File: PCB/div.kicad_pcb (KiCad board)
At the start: 2 copper layers, 31.5 x 110.5 mm, 74 parts, among them J1 Rst, J10 OUT, J2 Bus Gate Reset, J3 Clk, J4 PWR, J5 OUT, J6 OUT, J7 OUT, J8 OUT, J9 OUT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

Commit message: :memo: Change PCB text to v1.1
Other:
- board text added: "Control Board v1.1"
- board text removed: "Control Board v1"
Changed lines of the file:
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@@
   (gr_line (start 146.2 80.756) (end 146.5 80.756)
     (stroke (width 0.1) (type default)) (layer "Edge.Cuts"))
-  (gr_text "https://github.com/moPsy-project/div" (at 141.224 89.281 90) (layer "B.SilkS")
-    (effects (font (size 1 1) (thickness 0.15)) (justify left bottom mirror))
+  (gr_text "https://github.com/moPsy-project/div" (at 141.351 119.38 90) (layer "B.SilkS")
+    (effects (font (size 1 1) (thickness 0.15)) (justify right bottom mirror))
   )
   (gr_text "Jumper:\nBus Gate\nto Reset" (at 141.351 48.8 90) (layer "B.SilkS")
     (effects (font (size 1 1) (thickness 0.15)) (justify left bottom mirror))
   )
-  (gr_text "Control Board v1" (at 142.875 106.426 90) (layer "B.SilkS")
-    (effects (font (size 1 1) (thickness 0.15)) (justify left bottom mirror))
+  (gr_text "Control Board v1.1" (at 143.002 119.38 90) (layer "B.SilkS")
+    (effects (font (size 1 1) (thickness 0.15)) (justify right bottom mirror))
   )
-  (gr_text "Bend LEDs\nhere" (at 139.466 80.528) (layer "B.SilkS")
+  (gr_text "Bend LEDs\nhere" (at 139.573 80.137) (layer "B.SilkS")
     (effects (font (size 0.6 0.6) (thickness 0.1) bold) (justify bottom mirror))
   )
@@
   (segment (start 117.7032 79.0461) (end 124.7889 79.0461) (width 0.2032) (layer "F.Cu") (net 9))
   (segment (start 116.8 78.1429) (end 117.7032 79.0461) (width 0.2032) (layer "F.Cu") (net 9))
-  (segment (start 135.763 78.105) (end 134.2182 76.5602) (width 0.2032) (layer "B.Cu") (net 9))
-  (segment (start 128.0755 76.5602) (end 126.9282 75.4129) (width 0.2032) (layer "B.Cu") (net 9))
-  (segment (start 134.2182 76.5602) (end 128.0755 76.5602) (width 0.2032) (layer "B.Cu") (net 9))
+  (segment (start 128.2233 76.708) (end 126.9282 75.4129) (width 0.2032) (layer "B.Cu") (net 9))
+  (segment (start 135.763 78.105) (end 134.366 76.708) (width 0.2032) (layer "B.Cu") (net 9))
   (segment (start 135.763 79.248) (end 135.763 78.105) (width 0.2032) (layer "B.Cu") (net 9))
+  (segment (start 134.366 76.708) (end 128.2233 76.708) (width 0.2032) (layer "B.Cu") (net 9))
   (segment (start 130.683 74.041) (end 130.683 73.787) (width 0.2032) (layer "F.Cu") (net 10))
   (segment (start 125.825 73.9761) (end 126.9282 72.8729) (width 0.2032) (layer "F.Cu") (net 10))

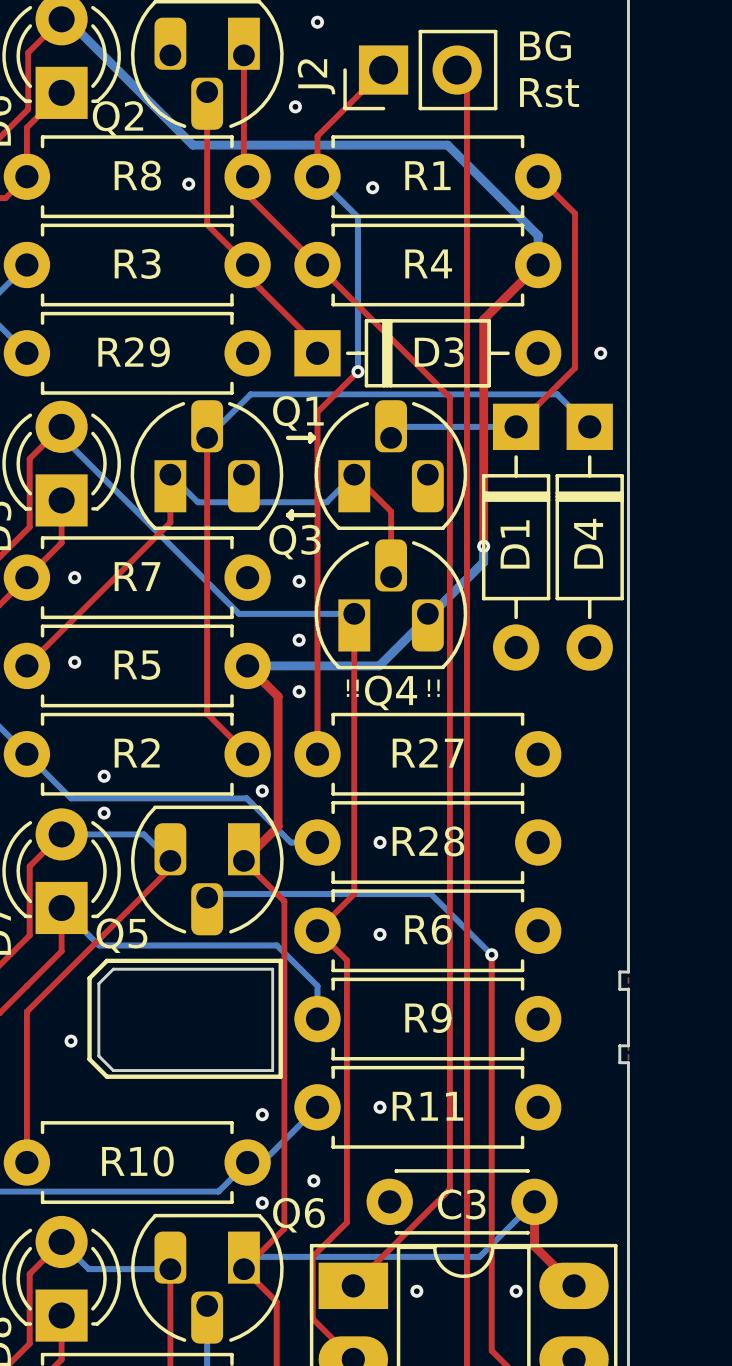
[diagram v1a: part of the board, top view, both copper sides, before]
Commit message: :art: Change the diode footprint to make soldering easier
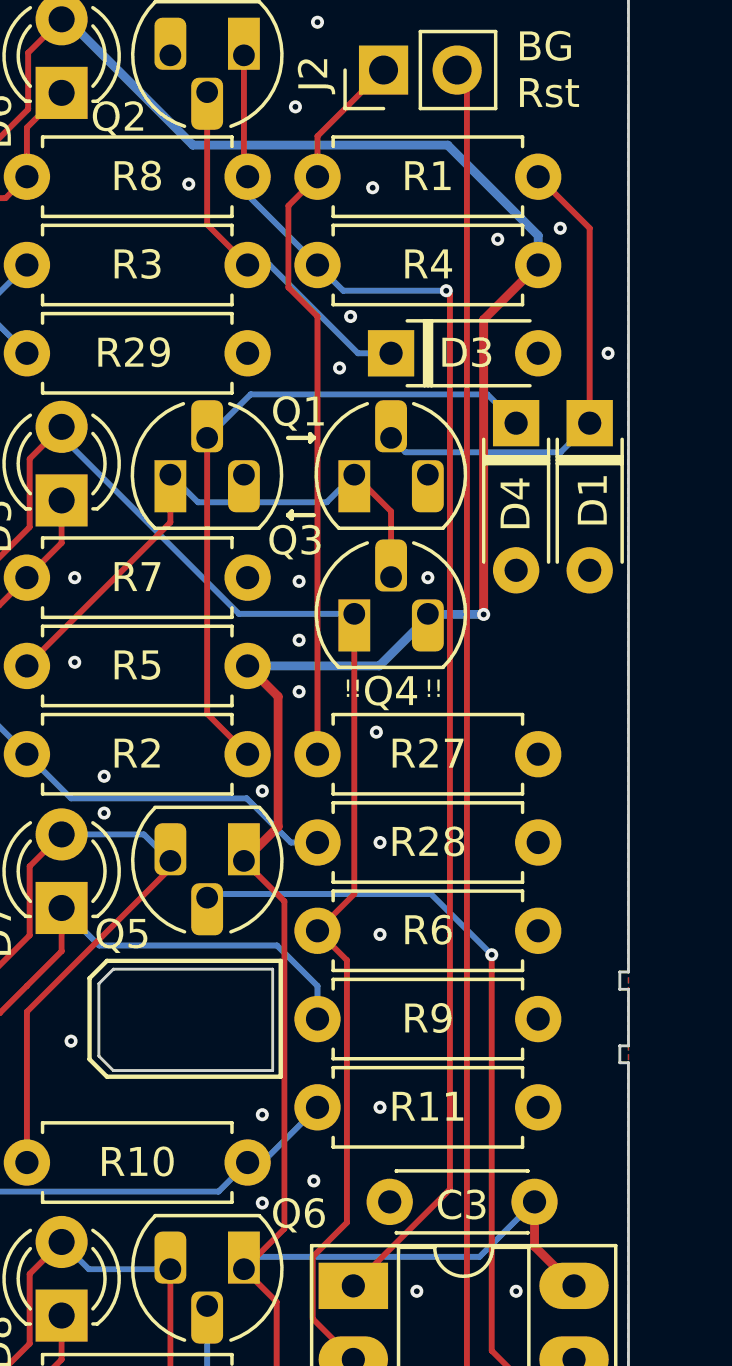
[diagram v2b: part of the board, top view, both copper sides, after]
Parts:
- D1, D3, D4: footprint Diode_THT:D_DO-35_SOD27_P7.62mm_Horizontal -> moPsy:D_DO-35_SOD27_P5.08mm_Horizontal
- moved D1 2.54 mm to (145.2, 58.7)
- moved D4 2.54 mm to (142.6, 58.7)
- moved D3 2.54 mm to (138.3, 56.3)
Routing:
- net Net-(D1-K): track 14.5 -> 17.3 mm
- net Net-(D4-K): track 25.8 -> 23.2 mm
- net Net-(D3-K): track 10.6 -> 12.7 mm
- net /CLOCK_IN: track 46.8 -> 48.9 mm, vias 0 -> 1
- net +12V: track 154.5 -> 155.6 mm
- net Net-(J2-Pin_1): track 25.7 -> 25.4 mm, vias 1 -> 0
- net GND: vias 58 -> 64

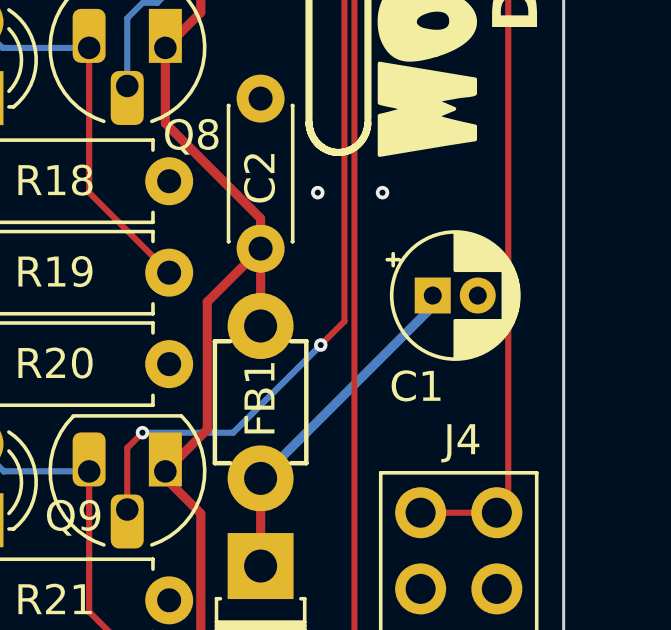
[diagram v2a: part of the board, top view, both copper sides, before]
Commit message: :art: Move C1 slightly for a more relaxed fit with the power connector
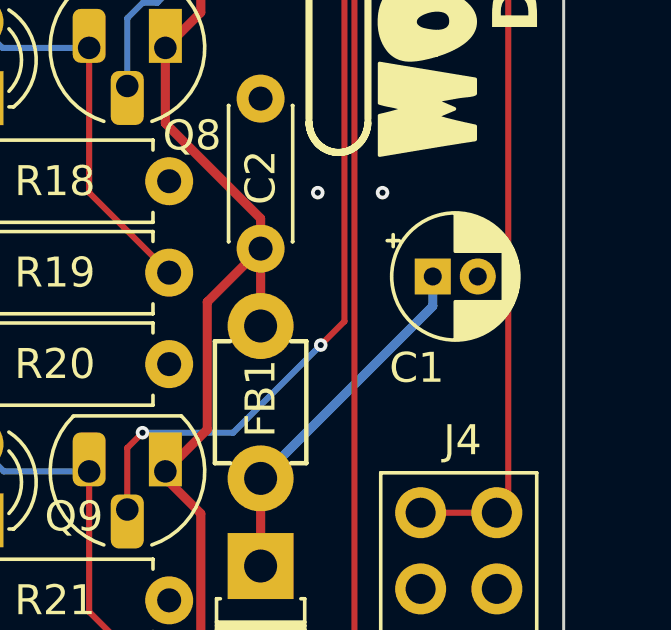
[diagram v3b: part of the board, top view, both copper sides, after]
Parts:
- moved C1 0.64 mm to (142.1, 123.6)
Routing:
- net Net-(D2-K): track 11.4 -> 12.0 mm
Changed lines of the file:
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@@
   )
   (footprint "Capacitor_THT:CP_Radial_D4.0mm_P1.50mm" (layer "F.Cu")
-    (at 142.137 124.206)
+    (at 142.137 123.571)
     (descr "CP, Radial series, Radial, pin pitch=1.50mm, , diameter=4mm, Electrolytic Capacitor")
     (tags "CP Radial series Radial pin pitch 1.50mm  diameter 4mm Electrolytic Capacitor")
@@
   )
   (segment (start 136.398 133.223) (end 136.398 130.302) (width 0.3048) (layer "F.Cu") (net 1))
-  (segment (start 142.137 124.563) (end 142.137 124.206) (width 0.3048) (layer "B.Cu") (net 1))
   (segment (start 136.398 130.302) (end 142.137 124.563) (width 0.3048) (layer "B.Cu") (net 1))
+  (segment (start 142.137 124.563) (end 142.137 123.571) (width 0.3048) (layer "B.Cu") (net 1))
   (via (at 122.936 122.174) (size 0.45) (drill 0.2) (layers "F.Cu" "B.Cu") (free) (net 2))
   (via (at 133.858 71.374) (size 0.45) (drill 0.2) (layers "F.Cu" "B.Cu") (free) (net 2))
